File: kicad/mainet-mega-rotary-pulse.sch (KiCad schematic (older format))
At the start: 16 parts, among them J100 Conn_01x01_Male, J103 Conn_01x04_Male, J104 Conn_01x01_Male, J105 Conn_01x01_Male, J65 Screw_Terminal_01x02, J66 Screw_Terminal_01x04, J99 Conn_01x01_Male, Q1 BUK9518-55, U1 4N38

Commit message: KICAD: Actualizar pin de entrada del Arduino-mega que recibe la señal del generador rotacional de pulsos
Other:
- note added: "D21"
- note removed: "D24"
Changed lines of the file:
@@
 	9450 3300 9450 3500
 Text Notes 10450 3600 0    50   ~ 0
-D24
+D21
 $EndSCHEMATC

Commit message: KICAD: Agregar imagenes del RPG al .sch
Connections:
- net VCC is gone; now on net GNDD: D22.2 (A), D23.1 (K), J66.1 (Pin_1), J66.3 (Pin_3), U1.5
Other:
- moved on the sheet: D21, D22, D23, J100, J103, J104, J105, J65, J66, J99, Q9, R17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

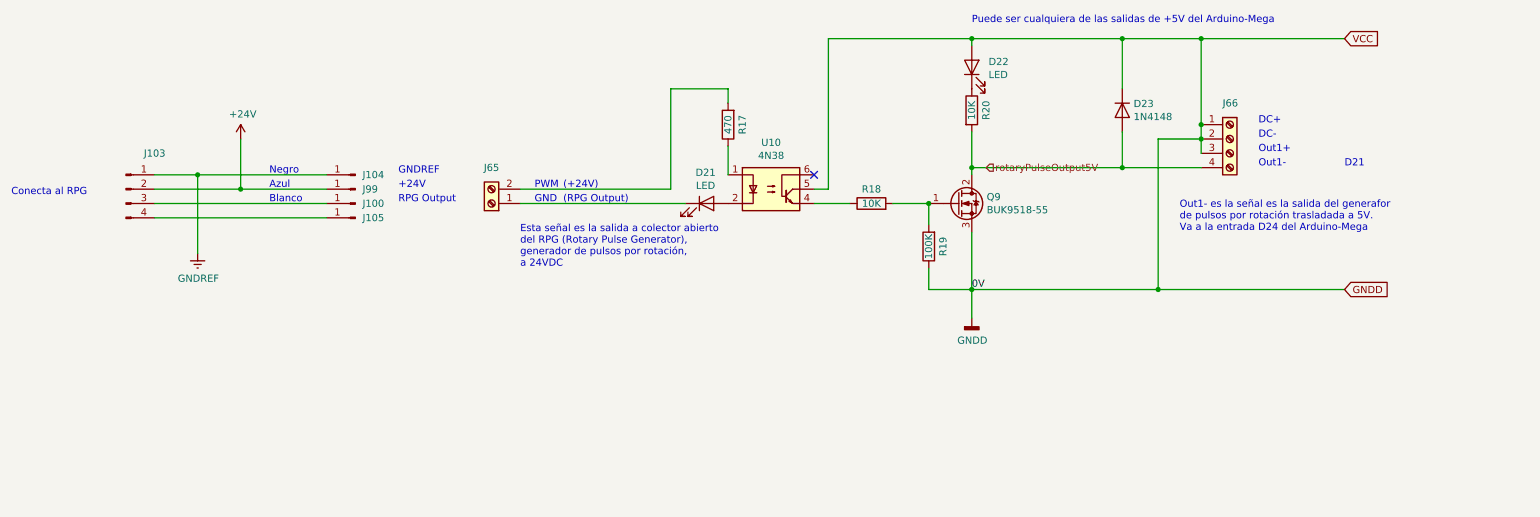
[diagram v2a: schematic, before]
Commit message: KICAD: Actualizar .sch del acondicionador de los pulsos del RPG de 24V a 5V
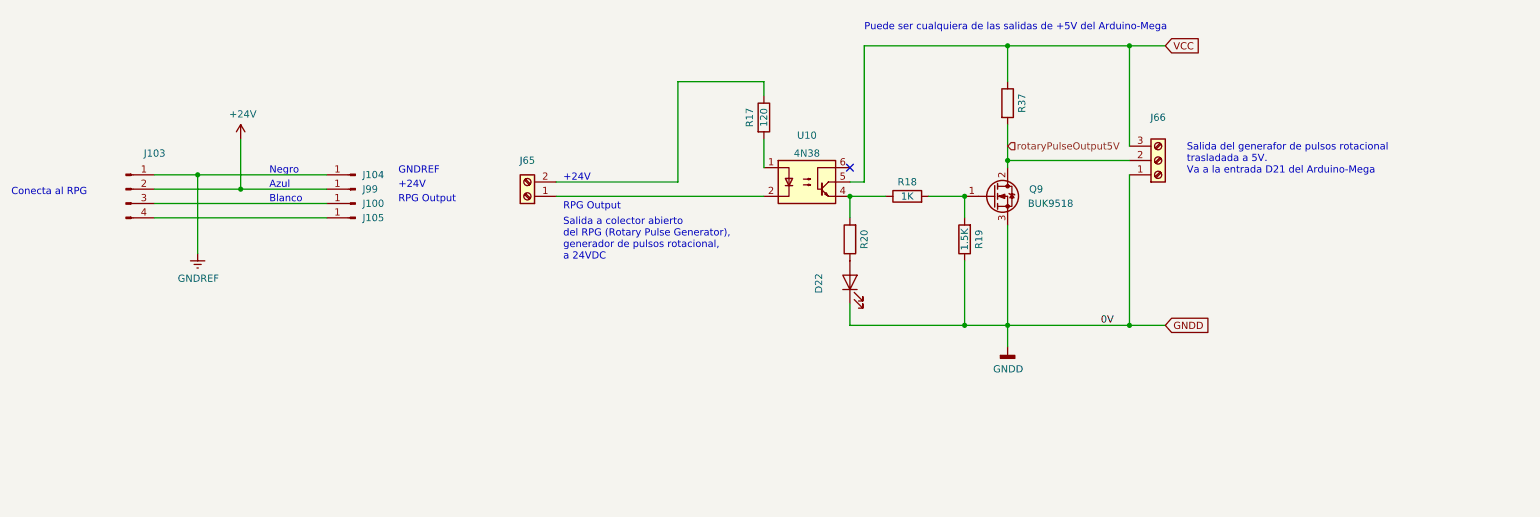
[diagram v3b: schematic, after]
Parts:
- removed D21: LED, symbol Device:LED
- removed D23: 1N4148, Diode_THT:D_DO-35_SOD27_P7.62mm_Horizontal, symbol Diode:1N4148
- removed J66: Screw_Terminal_01x04, symbol Connector:Screw_Terminal_01x04
- removed Q1: BUK9518-55, Package_TO_SOT_THT:TO-220-3_Vertical, symbol Transistor_FET:IRLZ44N
- removed R1: 470, Resistor_THT:R_Axial_DIN0414_L11.9mm_D4.5mm_P15.24mm_Horizontal, symbol Device:R
- removed R2: 10K, Resistor_THT:R_Axial_DIN0414_L11.9mm_D4.5mm_P15.24mm_Horizontal, symbol Device:R
- removed R3: 100K, Resistor_THT:R_Axial_DIN0414_L11.9mm_D4.5mm_P15.24mm_Horizontal, symbol Device:R
- removed R4: 10K, Resistor_THT:R_Axial_DIN0207_L6.3mm_D2.5mm_P10.16mm_Horizontal, symbol Device:R
- removed U1: 4N38, Package_DIP:DIP-6_W7.62mm, symbol Isolator:4N36
- added J66: ~, TerminalBlock_Altech:Altech_AK300_1x03_P5.00mm_45-Degree, symbol Connector:Screw_Terminal_01x03
- added Q9: BUK9518, Package_TO_SOT_THT:TO-220-3_Vertical, symbol Transistor_FET:IRLZ44N
- added R17: 120, Resistor_THT:R_Axial_DIN0207_L6.3mm_D2.5mm_P7.62mm_Horizontal, symbol Device:R
- added R18: 1K, Resistor_THT:R_Axial_DIN0207_L6.3mm_D2.5mm_P7.62mm_Horizontal, symbol Device:R
- added R19: 1.5K, Resistor_THT:R_Axial_DIN0207_L6.3mm_D2.5mm_P7.62mm_Horizontal, symbol Device:R
- added R20, R37: ~, Resistor_THT:R_Axial_DIN0207_L6.3mm_D2.5mm_P7.62mm_Horizontal, symbol Device:R
- added U10: 4N38, Package_DIP:DIP-6_W7.62mm, symbol Isolator:4N36
- D22: value LED -> ~; footprint (none) -> LED_THT:LED_D5.0mm
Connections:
- net GNDD: now also D22.1 (K), J66.1 (Pin_1), Q9.3 (S), R19.1; no longer D22.2 (A)
- net rotaryPulseOutput5V: now also J66.2 (Pin_2), Q9.2 (D), R37.2
- net at J65.2 (Pin_2): now also R17.1
- net at J65.1 (Pin_1): now also U10.2
- new net: Q9.1 (G), R18.2, R19.2
- new net: R17.2, U10.1
- new net: R18.1, R20.2, U10.4
- new net: D22.2 (A), R20.1
- new net VCC: J66.3 (Pin_3), R37.1, U10.5
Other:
- note added: "Salida a colector abierto\ndel RPG (Rotary Pulse Generator),\ngenerador de pulsos rotacional,\na 24VDC\n"
- note added: "Salida del generafor de pulsos rotacional\ntrasladada a 5V.\nVa a la entrada D21 del Arduino-Mega"
- note removed: "(+24V)"
- note removed: "(RPG Output)"
- note removed: "D21"
- note removed: "DC+"
- note removed: "DC-"
- note removed: "Esta señal es la salida a colector abierto\ndel RPG (Rotary Pulse Generator),\ngenerador de pulsos por rotación,\na 24VDC\n"
- note removed: "GND"
- note removed: "Out1+"
- note removed: "Out1-"
- note removed: "Out1- es la señal es la salida del generafor\nde pulsos por rotación trasladada a 5V.\nVa a la entrada D24 del Arduino-Mega"
- note removed: "PWM"
- moved on the sheet: J65
